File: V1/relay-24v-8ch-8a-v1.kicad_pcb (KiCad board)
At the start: 2 copper layers, 98 x 67.8 mm, 47 parts, among them J1 DB141V-2.54-2P, J2 DB141V-2.54-4P, J3 DB141V-2.54-4P, J4 DB142V-5.08-4P, J5 DB142V-5.08-4P, J6 DB142V-5.08-4P, J7 DB142V-5.08-4P, K1 G5Q-1A4-DC24V, K2 G5Q-1A4-DC24V, K3 G5Q-1A4-DC24V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

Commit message: Revising before manufacturing.
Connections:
- net /OUT1PW renamed /OUT1LN
- net /OUT2PW renamed /OUT2LN
- net /OUT3PW renamed /OUT3LN
- net /OUT4PW renamed /OUT4LN
- net /OUT5PW renamed /OUT5LN
- net /OUT6PW renamed /OUT6LN
- net /OUT7PW renamed /OUT7LN
- net /OUT8PW renamed /OUT8LN
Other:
- board text added: "LINE"
- board text removed: "V~"
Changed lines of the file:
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@@
 	(net 16 "/IN8")
 	(net 17 "/LED8")
-	(net 18 "/OUT1PW")
+	(net 18 "/OUT1LN")
 	(net 19 "/OUT2LD")
 	(net 20 "/OUT1LD")
-	(net 21 "/OUT2PW")
+	(net 21 "/OUT2LN")
 	(net 22 "/OUT3LD")
-	(net 23 "/OUT4PW")
-	(net 24 "/OUT3PW")
+	(net 23 "/OUT4LN")
+	(net 24 "/OUT3LN")
 	(net 25 "/OUT4LD")
 	(net 26 "/OUT6LD")
-	(net 27 "/OUT5PW")
-	(net 28 "/OUT6PW")
+	(net 27 "/OUT5LN")
+	(net 28 "/OUT6LN")
 	(net 29 "/OUT5LD")
 	(net 30 "/OUT7LD")
-	(net 31 "/OUT7PW")
-	(net 32 "/OUT8PW")
+	(net 31 "/OUT7LN")
+	(net 32 "/OUT8LN")
 	(net 33 "/OUT8LD")
 	(footprint "Tales:D_SOD-123"
@@
 			(layers "*.Cu" "*.Mask")
 			(remove_unused_layers no)
-			(net 27 "/OUT5PW")
+			(net 27 "/OUT5LN")
 			(pintype "passive")
 		)
@@
 			(layers "*.Cu" "*.Mask")
 			(remove_unused_layers no)
-			(net 24 "/OUT3PW")
+			(net 24 "/OUT3LN")
 			(pintype "passive")
 		)
@@
 			(layers "*.Cu" "*.Mask")
 			(remove_unused_layers no)
-			(net 28 "/OUT6PW")
+			(net 28 "/OUT6LN")
 			(pintype "passive")
 		)
@@
 			(layers "*.Cu" "*.Mask")
 			(remove_unused_layers no)
-			(net 18 "/OUT1PW")
+			(net 18 "/OUT1LN")
 			(pintype "passive")
 		)
@@
 			(layers "*.Cu" "*.Mask")
 			(remove_unused_layers no)
-			(net 31 "/OUT7PW")
+			(net 31 "/OUT7LN")
 			(pinfunction "Pin_1")
 			(pintype "passive")
@@
 			(layers "*.Cu" "*.Mask")
 			(remove_unused_layers no)
-			(net 31 "/OUT7PW")
+			(net 31 "/OUT7LN")
 			(pinfunction "Pin_1")
 			(pintype "passive")
@@
 			(layers "*.Cu" "*.Mask")
 			(remove_unused_layers no)
-			(net 32 "/OUT8PW")
+			(net 32 "/OUT8LN")
 			(pinfunction "Pin_3")
 			(pintype "passive")
@@
 			(layers "*.Cu" "*.Mask")
 			(remove_unused_layers no)
-			(net 32 "/OUT8PW")
+			(net 32 "/OUT8LN")
 			(pinfunction "Pin_3")
 			(pintype "passive")
@@
 			(layers "*.Cu" "*.Mask")
 			(remove_unused_layers no)
-			(net 28 "/OUT6PW")
+			(net 28 "/OUT6LN")
 			(pintype "passive")
 		)
@@
 			(layers "*.Cu" "*.Mask")
 			(remove_unused_layers no)
-			(net 18 "/OUT1PW")
+			(net 18 "/OUT1LN")
 			(pinfunction "Pin_1")
 			(pintype "passive")
@@
 			(layers "*.Cu" "*.Mask")
 			(remove_unused_layers no)
-			(net 18 "/OUT1PW")
+			(net 18 "/OUT1LN")
 			(pinfunction "Pin_1")
 			(pintype "passive")
@@
 			(layers "*.Cu" "*.Mask")
 			(remove_unused_layers no)
-			(net 21 "/OUT2PW")
+			(net 21 "/OUT2LN")
 			(pinfunction "Pin_3")
 			(pintype "passive")
@@
 			(layers "*.Cu" "*.Mask")
 			(remove_unused_layers no)
-			(net 21 "/OUT2PW")
+			(net 21 "/OUT2LN")
 			(pinfunction "Pin_3")
 			(pintype "passive")
@@
 			(layers "*.Cu" "*.Mask")
 			(remove_unused_layers no)
-			(net 27 "/OUT5PW")
+			(net 27 "/OUT5LN")
 			(pintype "passive")
 		)
@@
 			(layers "*.Cu" "*.Mask")
 			(remove_unused_layers no)
-			(net 23 "/OUT4PW")
+			(net 23 "/OUT4LN")
 			(pintype "passive")
 		)
@@
 			(layers "*.Cu" "*.Mask")
 			(remove_unused_layers no)
-			(net 21 "/OUT2PW")
+			(net 21 "/OUT2LN")
 			(pintype "passive")
 		)
@@
 			(layers "*.Cu" "*.Mask")
 			(remove_unused_layers no)
-			(net 32 "/OUT8PW")
+			(net 32 "/OUT8LN")
 			(pintype "passive")
 		)
@@
 			(layers "*.Cu" "*.Mask")
 			(remove_unused_layers no)
-			(net 18 "/OUT1PW")
+			(net 18 "/OUT1LN")
 			(pintype "passive")
 		)
@@
 			(layers "*.Cu" "*.Mask")
 			(remove_unused_layers no)
-			(net 31 "/OUT7PW")
+			(net 31 "/OUT7LN")
 			(pintype "passive")
 		)
@@
 			(layers "*.Cu" "*.Mask")
 			(remove_unused_layers no)
-			(net 32 "/OUT8PW")
+			(net 32 "/OUT8LN")
 			(pintype "passive")
 		)
@@
 			(layers "*.Cu" "*.Mask")
 			(remove_unused_layers no)
-			(net 24 "/OUT3PW")
+			(net 24 "/OUT3LN")
 			(pinfunction "Pin_1")
 			(pintype "passive")
@@
 			(layers "*.Cu" "*.Mask")
 			(remove_unused_layers no)
-			(net 24 "/OUT3PW")
+			(net 24 "/OUT3LN")
 			(pinfunction "Pin_1")
 			(pintype "passive")
@@
 			(layers "*.Cu" "*.Mask")
 			(remove_unused_layers no)
-			(net 23 "/OUT4PW")
+			(net 23 "/OUT4LN")
 			(pinfunction "Pin_3")
 			(pintype "passive")
@@
 			(layers "*.Cu" "*.Mask")
 			(remove_unused_layers no)
-			(net 23 "/OUT4PW")
+			(net 23 "/OUT4LN")
 			(pinfunction "Pin_3")
 			(pintype "passive")
@@
 			(layers "*.Cu" "*.Mask")
 			(remove_unused_layers no)
-			(net 27 "/OUT5PW")
+			(net 27 "/OUT5LN")
 			(pinfunction "Pin_1")
 			(pintype "passive")
@@
 			(layers "*.Cu" "*.Mask")
 			(remove_unused_layers no)
-			(net 27 "/OUT5PW")
+			(net 27 "/OUT5LN")
 			(pinfunction "Pin_1")
 			(pintype "passive")
@@
 			(layers "*.Cu" "*.Mask")
 			(remove_unused_layers no)
-			(net 28 "/OUT6PW")
+			(net 28 "/OUT6LN")
 			(pinfunction "Pin_3")
 			(pintype "passive")
@@
 			(layers "*.Cu" "*.Mask")
 			(remove_unused_layers no)
-			(net 28 "/OUT6PW")
+			(net 28 "/OUT6LN")
 			(pinfunction "Pin_3")
 			(pintype "passive")
@@
 			(layers "*.Cu" "*.Mask")
 			(remove_unused_layers no)
-			(net 24 "/OUT3PW")
+			(net 24 "/OUT3LN")
 			(pintype "passive")
 		)
@@
 			(layers "*.Cu" "*.Mask")
 			(remove_unused_layers no)
-			(net 23 "/OUT4PW")
+			(net 23 "/OUT4LN")
 			(pintype "passive")
 		)
@@
 			(layers "*.Cu" "*.Mask")
 			(remove_unused_layers no)
-			(net 21 "/OUT2PW")
+			(net 21 "/OUT2LN")
 			(pintype "passive")
 		)
@@
 			(layers "*.Cu" "*.Mask")
 			(remove_unused_layers no)
-			(net 31 "/OUT7PW")
+			(net 31 "/OUT7LN")
 			(pintype "passive")
 		)
@@
 		)
 	)
-	(gr_text "V~"
+	(gr_text "LINE"
 		(at 153 125.75 0)
 		(layer "F.SilkS")
@@
 		)
 	)
-	(gr_text "V~"
+	(gr_text "LINE"
 		(at 139.26 125.75 0)
 		(layer "F.SilkS")
@@
 		)
 	)
-	(gr_text "V~"
+	(gr_text "LINE"
 		(at 163.16 125.75 0)
 		(layer "F.SilkS")
@@
 		)
 	)
-	(gr_text "V~"
+	(gr_text "LINE"
 		(at 211.16 125.75 0)
 		(layer "F.SilkS")
@@
 		)
 	)
-	(gr_text "V~"
+	(gr_text "LINE"
 		(at 129.1 125.75 0)
 		(layer "F.SilkS")
@@
 		)
 	)
-	(gr_text "V~"
+	(gr_text "LINE"
 		(at 201 125.75 0)
 		(layer "F.SilkS")
@@
 		)
 	)
-	(gr_text "V~"
+	(gr_text "LINE"
 		(at 177.1 125.75 0)
 		(layer "F.SilkS")
@@
 		)
 	)
-	(gr_text "V~"
+	(gr_text "LINE"
 		(at 187.26 125.75 0)
 		(layer "F.SilkS")

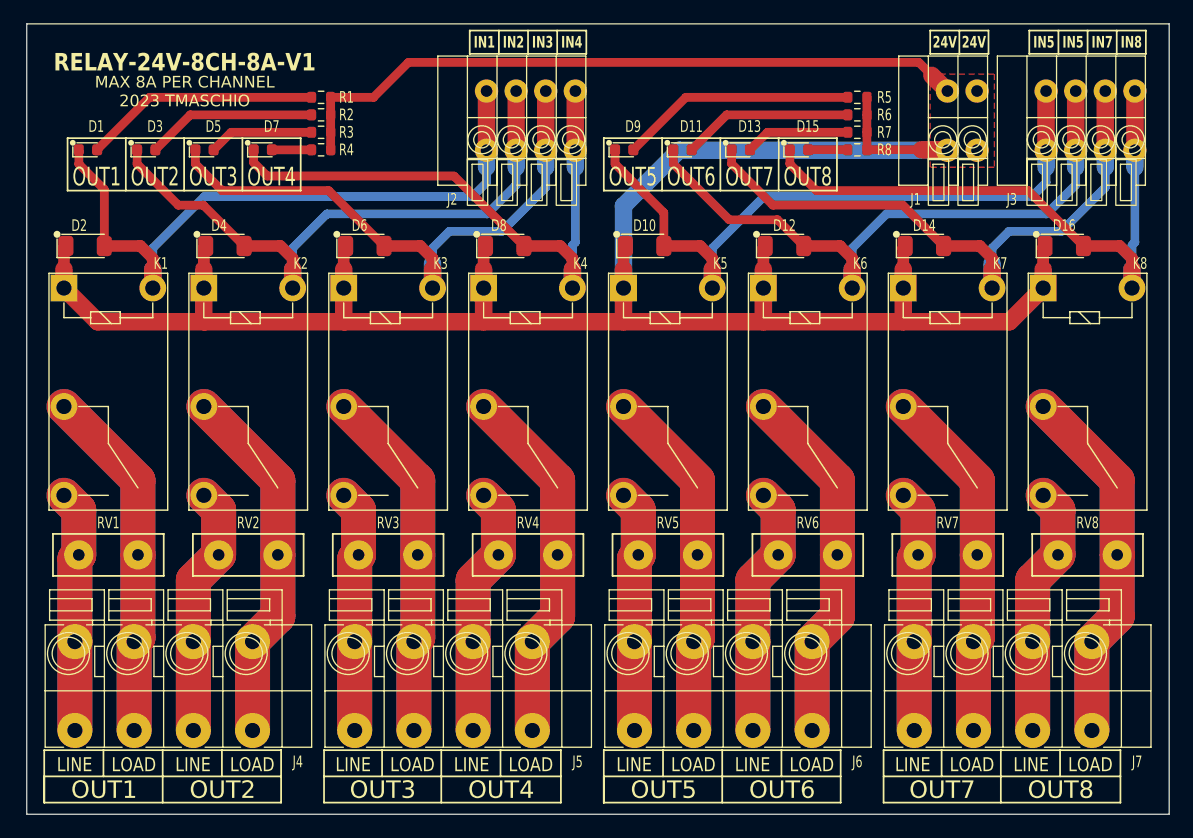
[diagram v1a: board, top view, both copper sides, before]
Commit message: Replaced input terminal blocks for 3.5mm pitch.
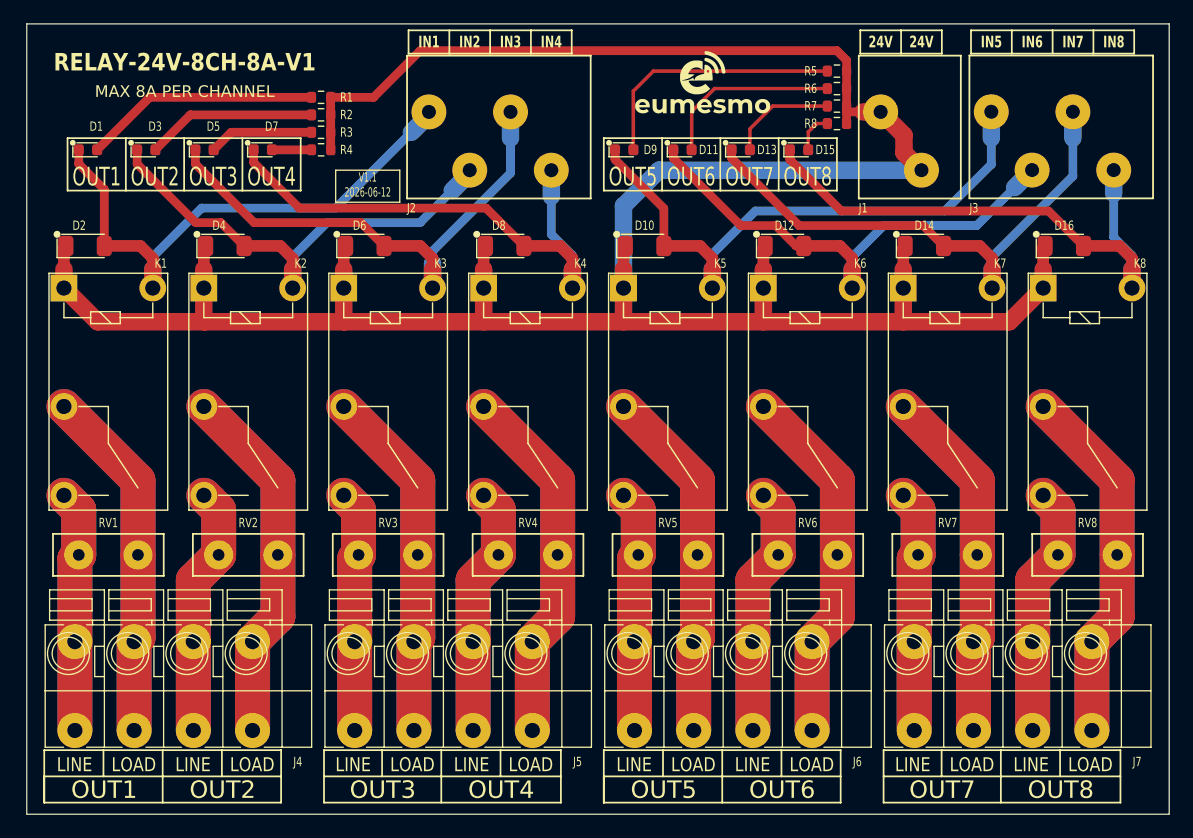
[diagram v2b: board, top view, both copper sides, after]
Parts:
- added G***: LOGO, Tales:Eumesmo_small_silk, F.Cu at (183.0, 67.2)
- J1: value DB141V-2.54-2P -> 250-202; footprint Tales:TerminalBlock_Dibo_DB141V-2.54-2P_1x02_P2.54mm_Vertical -> Tales:TerminalBlock_Wago_250-202_1x02_P3.5mm_45Degree
- J2, J3: value DB141V-2.54-4P -> 250-204; footprint Tales:TerminalBlock_Dibo_DB141V-2.54-4P_1x04_P2.54mm_Vertical -> Tales:TerminalBlock_Wago_250-204_1x04_P3.5mm_45Degree
- moved J1 5.53 mm to (200.0, 72.2)
- moved J2 3.91 mm to (164.8, 72.2)
- moved J3 3.69 mm to (213.0, 72.2)
- moved R5 2.85 mm to (194.5, 66.2)
- moved R6 2.85 mm to (194.5, 67.8)
- moved R7 2.85 mm to (194.5, 69.2)
- moved R8 2.85 mm to (194.5, 70.8)
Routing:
- net /IN2: track 53.4 -> 41.3 mm
- net /IN6: track 55.4 -> 43.4 mm
- net /IN1: track 58.5 -> 47.7 mm
- net +24V: track 241.1 -> 232.6 mm
- net /IN5: track 59.4 -> 51.7 mm
- net /IN8: track 53.5 -> 47.0 mm
- net /IN4: track 51.4 -> 45.0 mm
- net /IN3: track 51.0 -> 45.1 mm
- net /IN7: track 53.0 -> 47.2 mm
- net /LED5: track 20.3 -> 22.4 mm
- net /LED6: track 14.6 -> 15.7 mm
- removed copper zone on F.Cu, net +24V
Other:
- board text added: "IN6"
- board text added: "MAX 8A PER CHANNEL"
- board text added: "V1.1 2026-06-12"
- board text removed: "MAX 8A PER CHANNEL 2023 TMASCHIO"
